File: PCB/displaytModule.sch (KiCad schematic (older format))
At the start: 0 parts

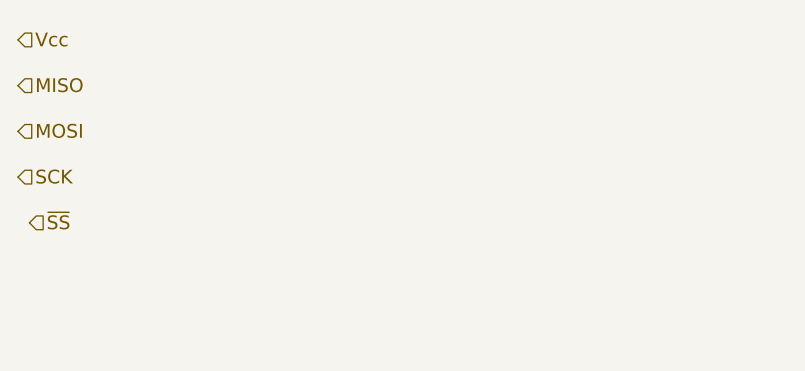
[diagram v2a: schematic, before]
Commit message: Added the symbol for the display module, which will actually be just a pin header
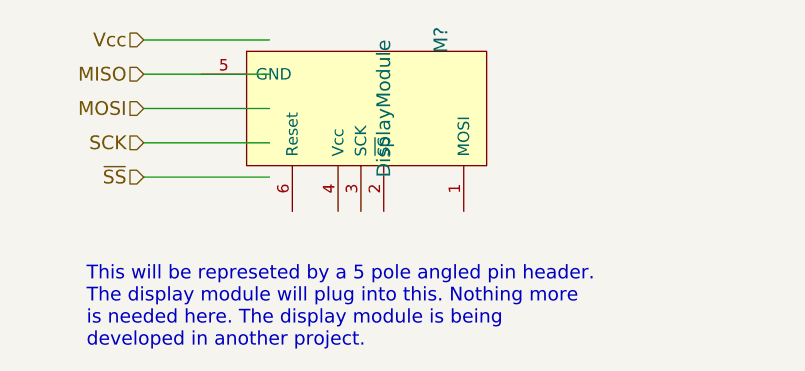
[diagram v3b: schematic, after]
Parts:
- added M?: DisplayModule, symbol DisplayModule
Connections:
- wire segments 0 -> 5
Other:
- note added: "This will be represeted by a 5 pole angled pin header. \nThe display module will plug into this. Nothing more\nis needed here. The display module is being \ndeveloped in another project."
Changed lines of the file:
@@
 Comment4 ""
 $EndDescr
-Text HLabel 2200 1850 2    60   Input ~ 0
+Text HLabel 2750 1800 0    60   Input ~ 0
 MISO
-Text HLabel 2200 2050 2    60   Input ~ 0
+Text HLabel 2750 1950 0    60   Input ~ 0
 MOSI
-Text HLabel 2200 2250 2    60   Input ~ 0
+Text HLabel 2750 2100 0    60   Input ~ 0
 SCK
-Text HLabel 2250 2450 2    60   Input ~ 0
+Text HLabel 2750 2250 0    60   Input ~ 0
 ~SS
-Text HLabel 2200 1650 2    60   Input ~ 0
+Text HLabel 2750 1650 0    60   Input ~ 0
 Vcc
+$Comp
+L DisplayModule M?
+U 1 1 559837A8
+P 3700 1950
+F 0 "M?" H 3400 2300 60  0000 C CNN
+F 1 "DisplayModule" H 3700 2050 60  0000 C CNN
+F 2 "" H 3700 1950 60  0000 C CNN
+F 3 "" H 3700 1950 60  0000 C CNN
+	1    3700 1950
+	0    1    1    0
+$EndComp
+Wire Wire Line
+	2750 1650 3300 1650
+Wire Wire Line
+	2750 1800 3300 1800
+Wire Wire Line
+	2750 1950 3300 1950
+Wire Wire Line
+	2750 2100 3300 2100
+Wire Wire Line
+	2750 2250 3300 2250
+Text Notes 2500 3000 0    60   ~ 0
+This will be represeted by a 5 pole angled pin header. \nThe display module will plug into this. Nothing more\nis needed here. The display module is being \ndeveloped in another project.
 $EndSCHEMATC

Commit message: Generated the Netlist and started associating footprints
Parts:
- M301: renamed from M?; footprint (none) -> Pin_Headers:Pin_Header_Angled_1x05
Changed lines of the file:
@@
 LIBS:valves
 LIBS:Tfac-Symbols
+LIBS:TfaC-cache
 EELAYER 25 0
 EELAYER END
@@
 Vcc
 $Comp
-L DisplayModule M?
+L DisplayModule M301
 U 1 1 559837A8
 P 3700 1950
-F 0 "M?" H 3400 2300 60  0000 C CNN
+F 0 "M301" V 4200 2200 60  0000 C CNN
 F 1 "DisplayModule" H 3700 2050 60  0000 C CNN
-F 2 "" H 3700 1950 60  0000 C CNN
+F 2 "Pin_Headers:Pin_Header_Angled_1x05" H 3700 1950 60  0001 C CNN
 F 3 "" H 3700 1950 60  0000 C CNN
 	1    3700 1950

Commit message: Started the layout
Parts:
- M301: footprint Pin_Headers:Pin_Header_Angled_1x05 -> Pin_Headers:Pin_Header_Straight_1x05
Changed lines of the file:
@@
 F 0 "M301" V 4200 2200 60  0000 C CNN
 F 1 "DisplayModule" H 3700 2050 60  0000 C CNN
-F 2 "Pin_Headers:Pin_Header_Angled_1x05" H 3700 1950 60  0001 C CNN
+F 2 "Pin_Headers:Pin_Header_Straight_1x05" H 3700 1950 60  0001 C CNN
 F 3 "" H 3700 1950 60  0000 C CNN
 	1    3700 1950

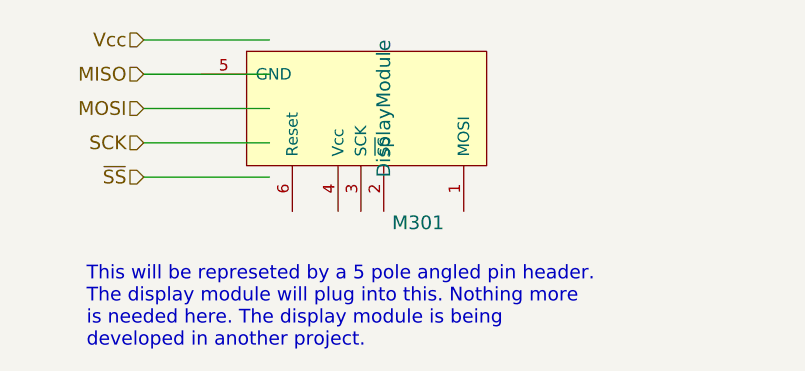
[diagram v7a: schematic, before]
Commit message: Added isolation resistors and corrected the reset connection
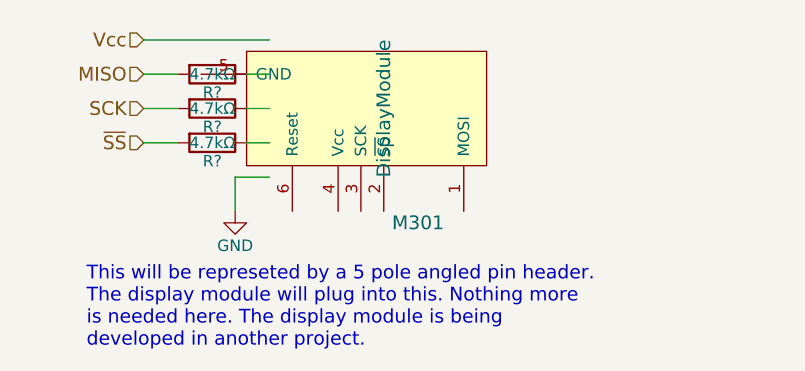
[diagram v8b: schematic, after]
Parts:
- added R? (x3): 4.7kΩ, symbol R
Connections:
- net labels added: GND
- net labels removed: MOSI
- wire segments 5 -> 9
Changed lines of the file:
@@
 LIBS:valves
 LIBS:Tfac-Symbols
-LIBS:TfaC-cache
 EELAYER 25 0
 EELAYER END
@@
 Text HLabel 2750 1800 0    60   Input ~ 0
 MISO
-Text HLabel 2750 1950 0    60   Input ~ 0
-MOSI
 Text HLabel 2750 2100 0    60   Input ~ 0
-SCK
-Text HLabel 2750 2250 0    60   Input ~ 0
 ~SS
 Text HLabel 2750 1650 0    60   Input ~ 0
@@
 	0    1    1    0
 $EndComp
+Text Notes 2500 3000 0    60   ~ 0
+This will be represeted by a 5 pole angled pin header. \nThe display module will plug into this. Nothing more\nis needed here. The display module is being \ndeveloped in another project.
+$Comp
+L R R?
+U 1 1 55F1C62E
+P 3050 1800
+F 0 "R?" V 3130 1800 50  0000 C CNN
+F 1 "4.7kΩ" V 3050 1800 50  0000 C CNN
+F 2 "" V 2980 1800 30  0000 C CNN
+F 3 "" H 3050 1800 30  0000 C CNN
+	1    3050 1800
+	0    1    1    0
+$EndComp
+$Comp
+L R R?
+U 1 1 55F1C655
+P 3050 1950
+F 0 "R?" V 3130 1950 50  0000 C CNN
+F 1 "4.7kΩ" V 3050 1950 50  0000 C CNN
+F 2 "" V 2980 1950 30  0000 C CNN
+F 3 "" H 3050 1950 30  0000 C CNN
+	1    3050 1950
+	0    1    1    0
+$EndComp
+$Comp
+L R R?
+U 1 1 55F1C67F
+P 3050 2100
+F 0 "R?" V 3130 2100 50  0000 C CNN
+F 1 "4.7kΩ" V 3050 2100 50  0000 C CNN
+F 2 "" V 2980 2100 30  0000 C CNN
+F 3 "" H 3050 2100 30  0000 C CNN
+	1    3050 2100
+	0    1    1    0
+$EndComp
 Wire Wire Line
 	2750 1650 3300 1650
 Wire Wire Line
-	2750 1800 3300 1800
+	2750 1800 2900 1800
 Wire Wire Line
-	2750 1950 3300 1950
+	3200 1800 3300 1800
 Wire Wire Line
-	2750 2100 3300 2100
+	2750 1950 2900 1950
 Wire Wire Line
-	2750 2250 3300 2250
-Text Notes 2500 3000 0    60   ~ 0
-This will be represeted by a 5 pole angled pin header. \nThe display module will plug into this. Nothing more\nis needed here. The display module is being \ndeveloped in another project.
+	3200 1950 3300 1950
+Wire Wire Line
+	2750 2100 2900 2100
+Wire Wire Line
+	3200 2100 3300 2100
+$Comp
+L GND #PWR?
+U 1 1 55F1C70D
+P 3150 2400
+F 0 "#PWR?" H 3150 2150 50  0001 C CNN
+F 1 "GND" H 3150 2250 50  0000 C CNN
+F 2 "" H 3150 2400 60  0000 C CNN
+F 3 "" H 3150 2400 60  0000 C CNN
+	1    3150 2400
+	1    0    0    -1
+$EndComp
+Wire Wire Line
+	3300 2250 3150 2250
+Wire Wire Line
+	3150 2250 3150 2400
+Text HLabel 2750 1950 0    60   Input ~ 0
+SCK
 $EndSCHEMATC
